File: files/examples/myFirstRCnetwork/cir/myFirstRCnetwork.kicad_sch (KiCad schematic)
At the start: 4 parts

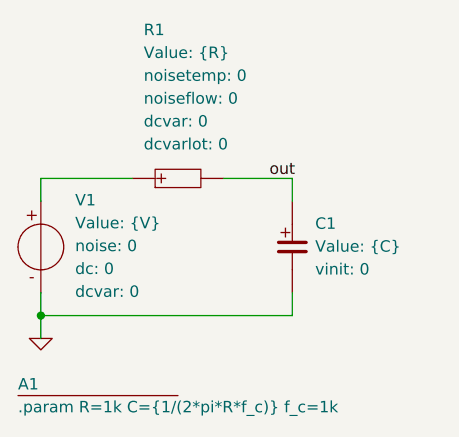
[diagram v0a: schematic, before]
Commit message: Updated KiCAD interface
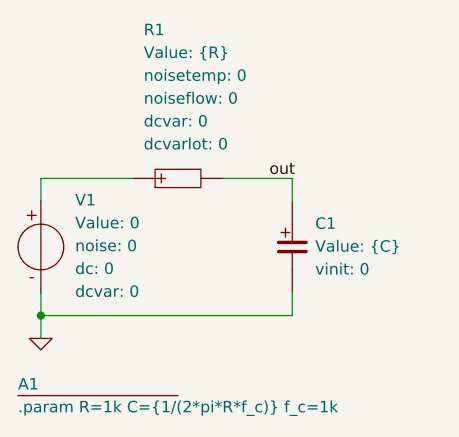
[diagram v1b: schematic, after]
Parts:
- V1: value {V} -> 0
